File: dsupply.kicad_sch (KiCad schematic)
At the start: 64 parts, among them J5 Barrel_Jack, Q2 BSS138, Q3 BSS138, Q4 BC857, Q5 AOSP21321, Q6 BC857, U21 ACPL-217-500E, U22 TPS54620, U23 AG5300, U24 PM1202, U25 AMS1117-3.3

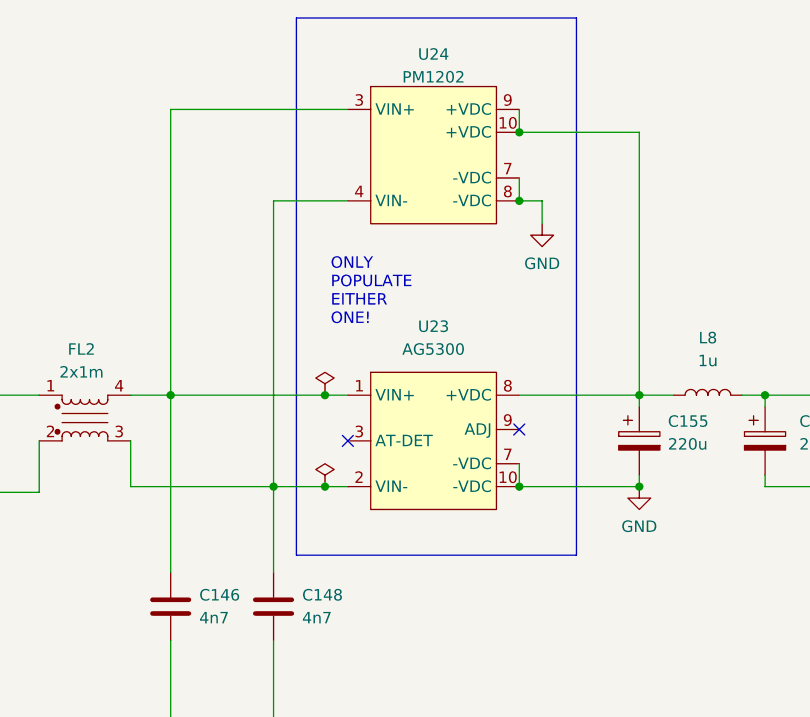
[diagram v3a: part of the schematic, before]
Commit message: change PD LD circuit
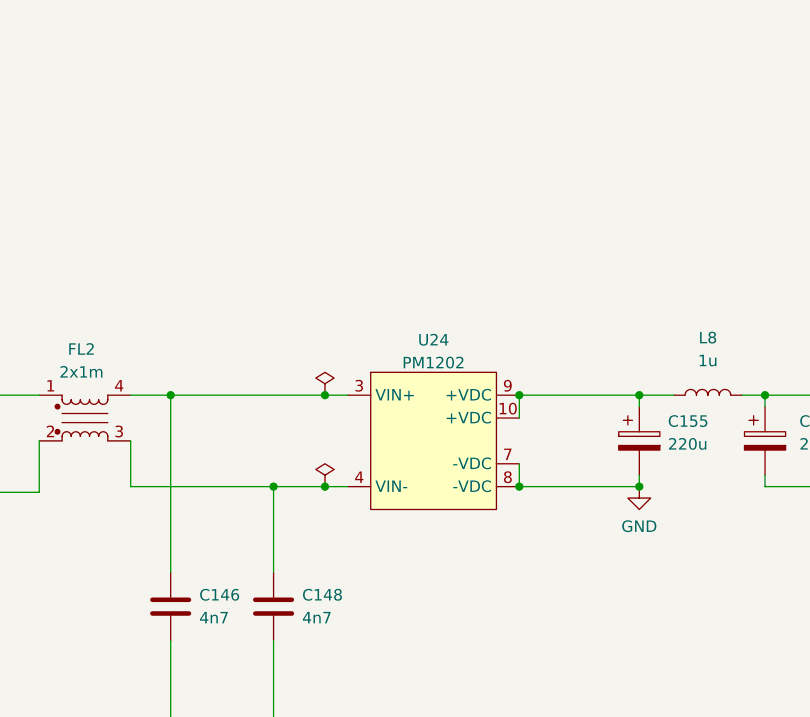
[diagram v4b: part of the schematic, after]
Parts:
- removed U23: AG5300, kirdy:AG5300, symbol kirdy:AG5300
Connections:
- no-connect marks 3 -> 1
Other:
- note removed: "ONLY POPULATE EITHER ONE!"
- moved on the sheet: U24
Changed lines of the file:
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@@
   (junction (at 87.63 149.86) (diameter 0) (color 0 0 0 0)
   )
-  (junction (at 199.39 54.61) (diameter 0) (color 0 0 0 0)
-  )
   (junction (at 212.725 86.36) (diameter 0) (color 0 0 0 0)
   )
+  (junction (at 199.39 86.36) (diameter 0) (color 0 0 0 0)
+  )
   (junction (at 364.49 157.48) (diameter 0) (color 0 0 0 0)
   )
@@
   (junction (at 123.19 149.86) (diameter 0) (color 0 0 0 0)
   )
-  (junction (at 199.39 46.99) (diameter 0) (color 0 0 0 0)
-  )
   (junction (at 73.66 149.86) (diameter 0) (color 0 0 0 0)
   )
+  (junction (at 199.39 76.2) (diameter 0) (color 0 0 0 0)
+  )
   (junction (at 341.63 76.2) (diameter 0) (color 0 0 0 0)
   )
@@
   (junction (at 172.72 157.48) (diameter 0) (color 0 0 0 0)
   )
-  (junction (at 199.39 86.36) (diameter 0) (color 0 0 0 0)
-  )
   (junction (at 264.16 157.48) (diameter 0) (color 0 0 0 0)
   )
-  (no_connect (at 180.34 81.28))
-  (no_connect (at 199.39 80.01))
   (no_connect (at 147.32 162.56))
   (wire (pts (xy 224.155 76.2) (xy 226.695 76.2))
@@
     (stroke (width 0) (type default) (color 0 0 0 0))
   )
-  (polyline (pts (xy 205.74 93.98) (xy 205.74 34.29))
-    (stroke (width 0) (type default) (color 0 0 0 0))
-  )
   (wire (pts (xy 147.32 149.86) (xy 147.32 152.4))
     (stroke (width 0) (type default) (color 0 0 0 0))
@@
     (stroke (width 0) (type default) (color 0 0 0 0))
   )
-  (wire (pts (xy 199.39 54.61) (xy 201.93 54.61))
-    (stroke (width 0) (type default) (color 0 0 0 0))
-  )
   (wire (pts (xy 251.46 182.88) (xy 251.46 173.99))
     (stroke (width 0) (type default) (color 0 0 0 0))
@@
     (stroke (width 0) (type default) (color 0 0 0 0))
   )
-  (wire (pts (xy 160.655 44.45) (xy 160.655 76.2))
-    (stroke (width 0) (type default) (color 0 0 0 0))
-  )
   (wire (pts (xy 55.88 93.98) (xy 64.77 93.98))
     (stroke (width 0) (type default) (color 0 0 0 0))
@@
     (stroke (width 0) (type default) (color 0 0 0 0))
   )
-  (polyline (pts (xy 174.625 93.98) (xy 205.74 93.98))
-    (stroke (width 0) (type default) (color 0 0 0 0))
-  )
   (wire (pts (xy 334.01 76.2) (xy 341.63 76.2))
     (stroke (width 0) (type default) (color 0 0 0 0))
   )
-  (wire (pts (xy 180.34 44.45) (xy 160.655 44.45))
-    (stroke (width 0) (type default) (color 0 0 0 0))
-  )
   (wire (pts (xy 341.63 76.2) (xy 341.63 78.74))
     (stroke (width 0) (type default) (color 0 0 0 0))
@@
     (stroke (width 0) (type default) (color 0 0 0 0))
   )
-  (wire (pts (xy 199.39 44.45) (xy 199.39 46.99))
-    (stroke (width 0) (type default) (color 0 0 0 0))
-  )
   (wire (pts (xy 90.17 88.9) (xy 90.17 100.33))
     (stroke (width 0) (type default) (color 0 0 0 0))
@@
     (stroke (width 0) (type default) (color 0 0 0 0))
   )
-  (wire (pts (xy 212.725 46.99) (xy 212.725 76.2))
-    (stroke (width 0) (type default) (color 0 0 0 0))
-  )
   (wire (pts (xy 100.965 93.98) (xy 100.965 100.33))
     (stroke (width 0) (type default) (color 0 0 0 0))
@@
     (stroke (width 0) (type default) (color 0 0 0 0))
   )
-  (polyline (pts (xy 174.625 34.29) (xy 205.74 34.29))
-    (stroke (width 0) (type default) (color 0 0 0 0))
-  )
   (wire (pts (xy 363.855 88.265) (xy 363.855 81.28))
     (stroke (width 0) (type default) (color 0 0 0 0))
@@
     (stroke (width 0) (type default) (color 0 0 0 0))
   )
-  (polyline (pts (xy 174.625 34.29) (xy 174.625 93.98))
-    (stroke (width 0) (type default) (color 0 0 0 0))
-  )
   (wire (pts (xy 297.18 109.22) (xy 297.18 111.125))
     (stroke (width 0) (type default) (color 0 0 0 0))
@@
     (stroke (width 0) (type default) (color 0 0 0 0))
   )
+  (wire (pts (xy 199.39 76.2) (xy 199.39 78.74))
+    (stroke (width 0) (type default) (color 0 0 0 0))
+  )
   (wire (pts (xy 317.5 165.1) (xy 336.55 165.1))
     (stroke (width 0) (type default) (color 0 0 0 0))
@@
     (stroke (width 0) (type default) (color 0 0 0 0))
   )
-  (wire (pts (xy 172.085 54.61) (xy 180.34 54.61))
-    (stroke (width 0) (type default) (color 0 0 0 0))
-  )
   (wire (pts (xy 226.695 77.47) (xy 226.695 76.2))
     (stroke (width 0) (type default) (color 0 0 0 0))
@@
     (stroke (width 0) (type default) (color 0 0 0 0))
   )
-  (wire (pts (xy 199.39 46.99) (xy 212.725 46.99))
-    (stroke (width 0) (type default) (color 0 0 0 0))
-  )
   (wire (pts (xy 240.03 173.99) (xy 240.03 182.88))
     (stroke (width 0) (type default) (color 0 0 0 0))
@@
     (stroke (width 0) (type default) (color 0 0 0 0))
   )
-  (wire (pts (xy 201.93 54.61) (xy 201.93 57.15))
-    (stroke (width 0) (type default) (color 0 0 0 0))
-  )
   (wire (pts (xy 226.695 86.36) (xy 226.695 85.09))
     (stroke (width 0) (type default) (color 0 0 0 0))
@@
     (stroke (width 0) (type default) (color 0 0 0 0))
   )
-  (wire (pts (xy 172.085 86.36) (xy 172.085 54.61))
-    (stroke (width 0) (type default) (color 0 0 0 0))
-  )
   (wire (pts (xy 167.64 167.64) (xy 181.61 167.64))
     (stroke (width 0) (type default) (color 0 0 0 0))
@@
     (stroke (width 0) (type default) (color 0 0 0 0))
   )
-  (wire (pts (xy 199.39 52.07) (xy 199.39 54.61))
-    (stroke (width 0) (type default) (color 0 0 0 0))
-  )
   (wire (pts (xy 85.725 71.755) (xy 90.17 71.755))
     (stroke (width 0) (type default) (color 0 0 0 0))
@@
   (wire (pts (xy 336.55 165.1) (xy 351.79 165.1))
     (stroke (width 0) (type default) (color 0 0 0 0))
-  )
-  (text "ONLY \nPOPULATE\nEITHER\nONE!" (at 178.435 68.58 0)
-    (effects (font (size 1.27 1.27)) (justify left bottom))
   )
   (hierarchical_label "POE_PWR_SRC" (shape output) (at 279.4 83.82 0)
@@
     (pin "2")
   )
-  (symbol (lib_id "kirdy:PM1202") (at 189.23 52.07 0) (unit 1)
-    (in_bom yes) (on_board yes) (fields_autoplaced)
-    (property "Reference" "U24" (id 0) (at 189.865 38.3372 0))
-    (property "Value" "PM1202" (id 1) (at 189.865 40.8741 0))
-    (property "Footprint" "kirdy:PM1202" (id 2) (at 167.64 36.83 0)
-      (effects (font (size 1.27 1.27)) hide)
-    )
-    (property "Datasheet" "" (id 3) (at 167.64 36.83 0)
+  (symbol (lib_id "kirdy:PM1202") (at 189.23 83.82 0) (unit 1)
+    (in_bom yes) (on_board yes) (fields_autoplaced)
+    (property "Reference" "U24" (id 0) (at 189.865 70.0872 0))
+    (property "Value" "PM1202" (id 1) (at 189.865 72.6241 0))
+    (property "Footprint" "kirdy:PM1202" (id 2) (at 167.64 68.58 0)
+      (effects (font (size 1.27 1.27)) hide)
+    )
+    (property "Datasheet" "" (id 3) (at 167.64 68.58 0)
       (effects (font (size 1.27 1.27)) hide)
     )
@@
     (pin "2")
   )
-  (symbol (lib_id "kirdy:AG5300") (at 189.23 83.82 0) (unit 1)
-    (in_bom yes) (on_board yes) (fields_autoplaced)
-    (property "Reference" "U23" (id 0) (at 189.865 68.58 0))
-    (property "Value" "AG5300" (id 1) (at 189.865 71.12 0))
-    (property "Footprint" "kirdy:AG5300" (id 2) (at 167.64 68.58 0)
-      (effects (font (size 1.27 1.27)) hide)
-    )
-    (property "Datasheet" "https://silvertel.com/images/datasheets/Ag5300-datasheet-smallest-30W-Power-Over-Ethernet-Plus-Module-PoEplusPD.pdf" (id 3) (at 167.64 68.58 0)
-      (effects (font (size 1.27 1.27)) hide)
-    )
-    (property "MFR_PN" "AG5300" (id 4) (at 189.23 83.82 0)
-      (effects (font (size 1.27 1.27)) hide)
-    )
-    (pin "1")
-    (pin "10")
-    (pin "2")
-    (pin "3")
-    (pin "4")
-    (pin "5")
-    (pin "6")
-    (pin "7")
-    (pin "8")
-    (pin "9")
-  )
   (symbol (lib_id "power:GND") (at 73.66 170.18 0) (unit 1)
     (in_bom yes) (on_board yes) (fields_autoplaced)
@@
     (pin "2")
   )
-  (symbol (lib_id "power:GND") (at 201.93 57.15 0) (unit 1)
-    (in_bom yes) (on_board yes) (fields_autoplaced)
-    (property "Reference" "#PWR0165" (id 0) (at 201.93 63.5 0)
-      (effects (font (size 1.27 1.27)) hide)
-    )
-    (property "Value" "GND" (id 1) (at 201.93 61.5934 0))
-    (property "Footprint" "" (id 2) (at 201.93 57.15 0)
-      (effects (font (size 1.27 1.27)) hide)
-    )
-    (property "Datasheet" "" (id 3) (at 201.93 57.15 0)
-      (effects (font (size 1.27 1.27)) hide)
-    )
-    (pin "1")
-  )
   (symbol (lib_id "power:+12V") (at 53.34 149.86 90) (unit 1)

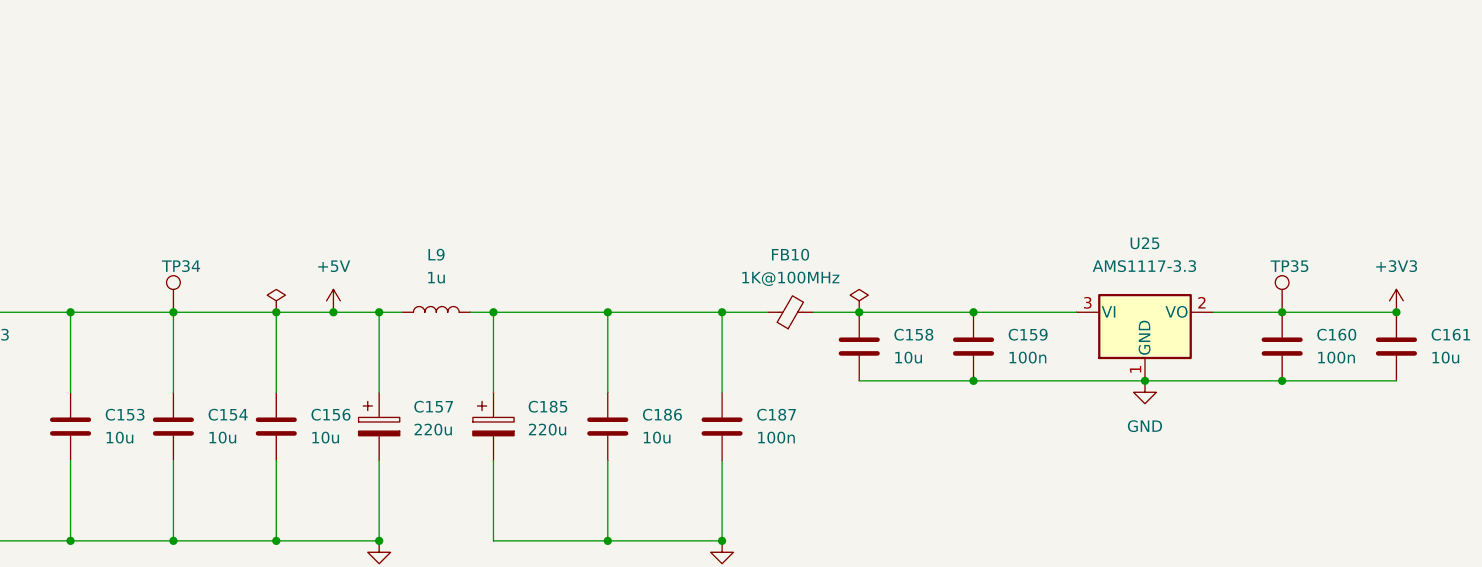
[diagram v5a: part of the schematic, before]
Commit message: import sch to pcb
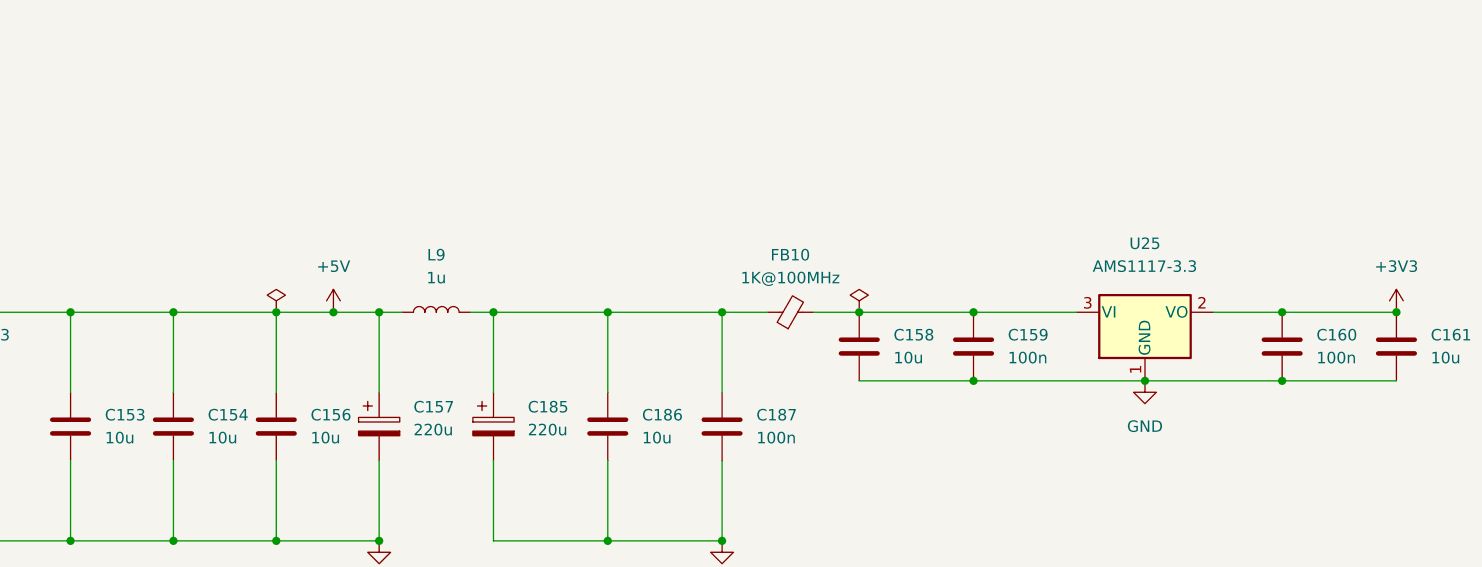
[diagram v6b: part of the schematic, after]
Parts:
- removed TP34, TP35: TestPoint, TestPoint:TestPoint_Pad_2.0x2.0mm, symbol Connector:TestPoint
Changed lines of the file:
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@@
     (pin "2")
-  )
-  (symbol (lib_id "Connector:TestPoint") (at 228.6 157.48 0) (unit 1)
-    (in_bom yes) (on_board yes)
-    (property "Reference" "TP34" (id 0) (at 227.33 152.4 0)
-      (effects (font (size 1.27 1.27)) (justify left))
-    )
-    (property "Value" "TestPoint" (id 1) (at 229.997 155.8802 0)
-      (effects (font (size 1.27 1.27)) (justify left) hide)
-    )
-    (property "Footprint" "TestPoint:TestPoint_Pad_2.0x2.0mm" (id 2) (at 233.68 157.48 0)
-      (effects (font (size 1.27 1.27)) hide)
-    )
-    (property "Datasheet" "~" (id 3) (at 233.68 157.48 0)
-      (effects (font (size 1.27 1.27)) hide)
-    )
-    (pin "1")
   )
   (symbol (lib_id "power:+5V") (at 246.38 157.48 0) (unit 1)
@@
     (pin "2")
   )
-  (symbol (lib_id "Connector:TestPoint") (at 351.79 157.48 0) (unit 1)
-    (in_bom yes) (on_board yes)
-    (property "Reference" "TP35" (id 0) (at 350.52 152.4 0)
-      (effects (font (size 1.27 1.27)) (justify left))
-    )
-    (property "Value" "TestPoint" (id 1) (at 353.187 155.8802 0)
-      (effects (font (size 1.27 1.27)) (justify left) hide)
-    )
-    (property "Footprint" "TestPoint:TestPoint_Pad_2.0x2.0mm" (id 2) (at 356.87 157.48 0)
-      (effects (font (size 1.27 1.27)) hide)
-    )
-    (property "Datasheet" "~" (id 3) (at 356.87 157.48 0)
-      (effects (font (size 1.27 1.27)) hide)
-    )
-    (pin "1")
-  )
   (symbol (lib_id "Device:R") (at 135.89 104.14 0) (unit 1)

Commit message: sync
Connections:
- net +12V: now also C181.1, C182.1, C183.1, C184.1, L8.2; no longer D9.1 (A1), J5.1, Q5.1 (S), Q5.2 (S), Q5.3 (S), Q6.2 (E)
- net at Q4.2 (E), Q5.5 (D), Q5.6 (D)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: now also C155.1, U24.10 (+VDC), U24.9 (+VDC); no longer C181.1, C182.1, C183.1, C184.1, L8.2
- new net: D9.1 (A1), J5.1, L8.1, Q5.1 (S), Q5.2 (S), Q5.3 (S), Q6.2 (E)
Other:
- moved on the sheet: C181, C182, C183, C184, D9, J5, L8, Q4, Q5, Q6, R68, R69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

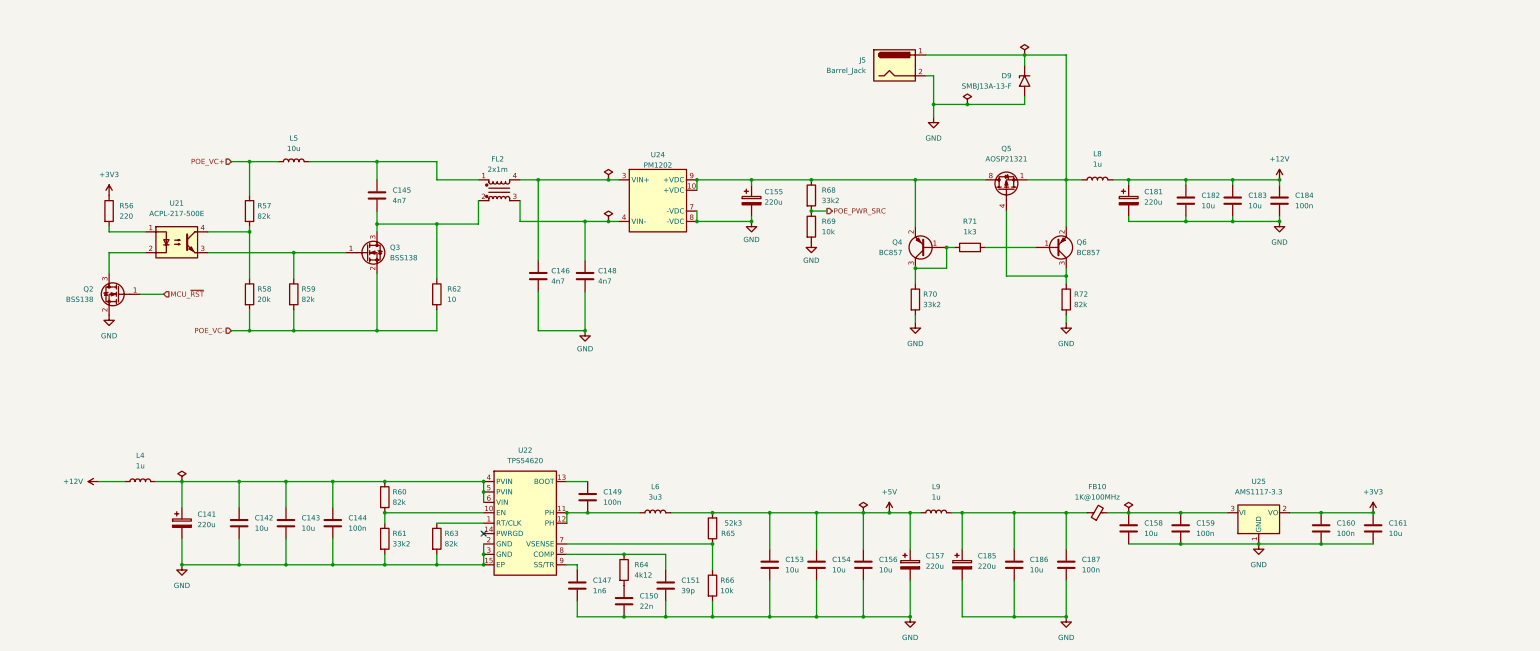
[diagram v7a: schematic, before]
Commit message: improve relay power circuitry
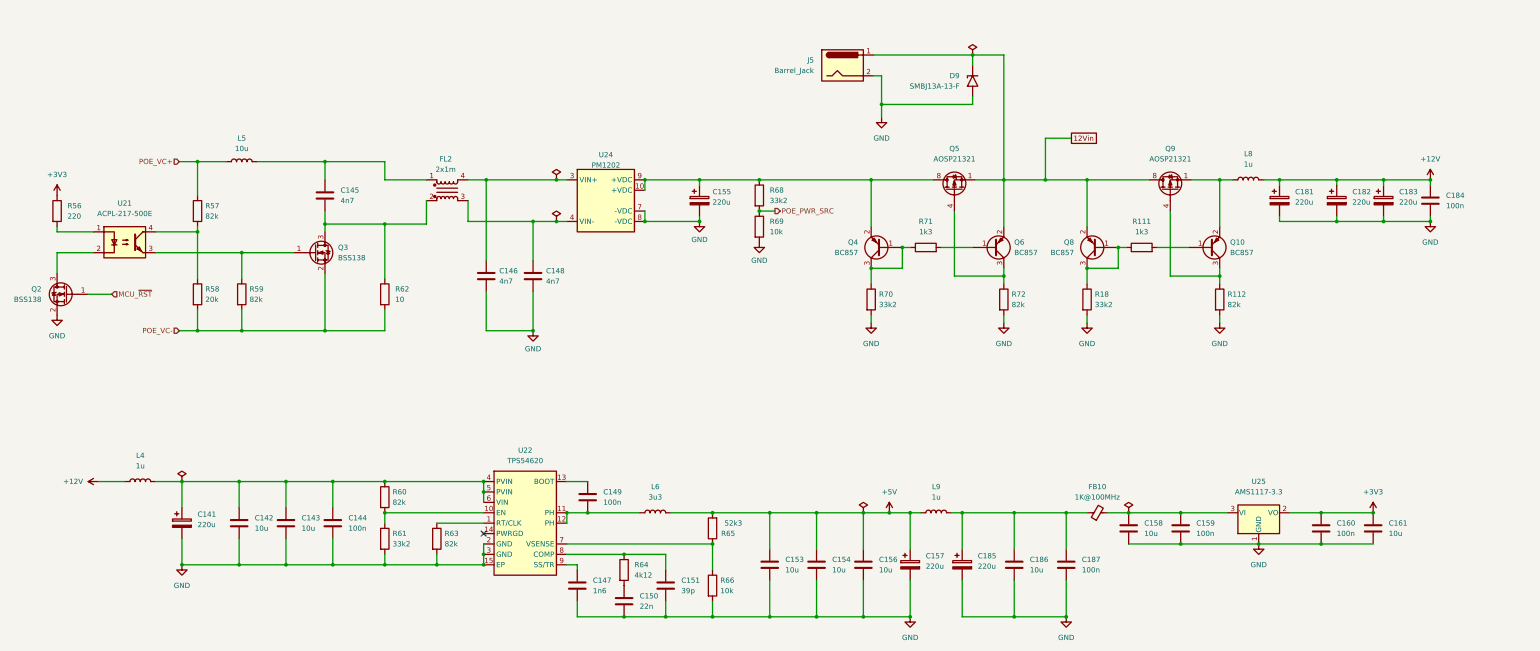
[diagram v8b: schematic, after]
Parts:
- removed C182, C183: 10u, Capacitor_SMD:C_0805_2012Metric, symbol Device:C
- added C182, C183: 220u, Capacitor_Tantalum_SMD:CP_EIA-7343-15_Kemet-W, symbol Device:C_Polarized
- added Q10, Q8: BC857, Package_TO_SOT_SMD:SOT-23, symbol Transistor_BJT:BC857
- added Q9: AOSP21321, Package_SO:SOIC-8_3.9x4.9mm_P1.27mm, symbol Transistor_FET:FDS9435A
- added R111: 1k3, Resistor_SMD:R_0603_1608Metric, symbol Device:R
- added R112: 82k, Resistor_SMD:R_0603_1608Metric, symbol Device:R
- added R18: 33k2, Resistor_SMD:R_0603_1608Metric, symbol Device:R
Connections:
- net +12V: now also C182.1, C183.1
- net GND: now also C182.2, C183.2, R112.2, R18.2
- net 12Vin: now reaches D9.1 (A1), J5.1, Q5.1 (S), Q5.2 (S), Q5.3 (S), Q6.2 (E)
- net 12Vin: now also Q8.2 (E), Q9.5 (D), Q9.6 (D), Q9.7 (D), Q9.8 (D); no longer L8.1
- new net: Q8.1 (B), Q8.3 (C), R111.1, R18.1
- new net: Q10.1 (B), R111.2
- new net: L8.1, Q10.2 (E), Q9.1 (S), Q9.2 (S), Q9.3 (S)
- new net: Q10.3 (C), Q9.4 (G), R112.1
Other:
- moved on the sheet: C145, C146, C148, C155, C181, C184, D9, FL2, J5, L5, L8, Q2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
